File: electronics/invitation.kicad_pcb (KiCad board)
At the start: 2 copper layers, 86 x 57 mm, 53 parts, among them P1 USB Micro B, P10 Up Arrow, P11 Down Arrow, P2 Home btn, P3 Bottom Connections 1, P4 Left Arrow, P5 Right Arrow, P8 CONN_01X01, P9 CONN_01X02, U1 ATMEGA32U4-A, Y1 16 FA-238 Mhz

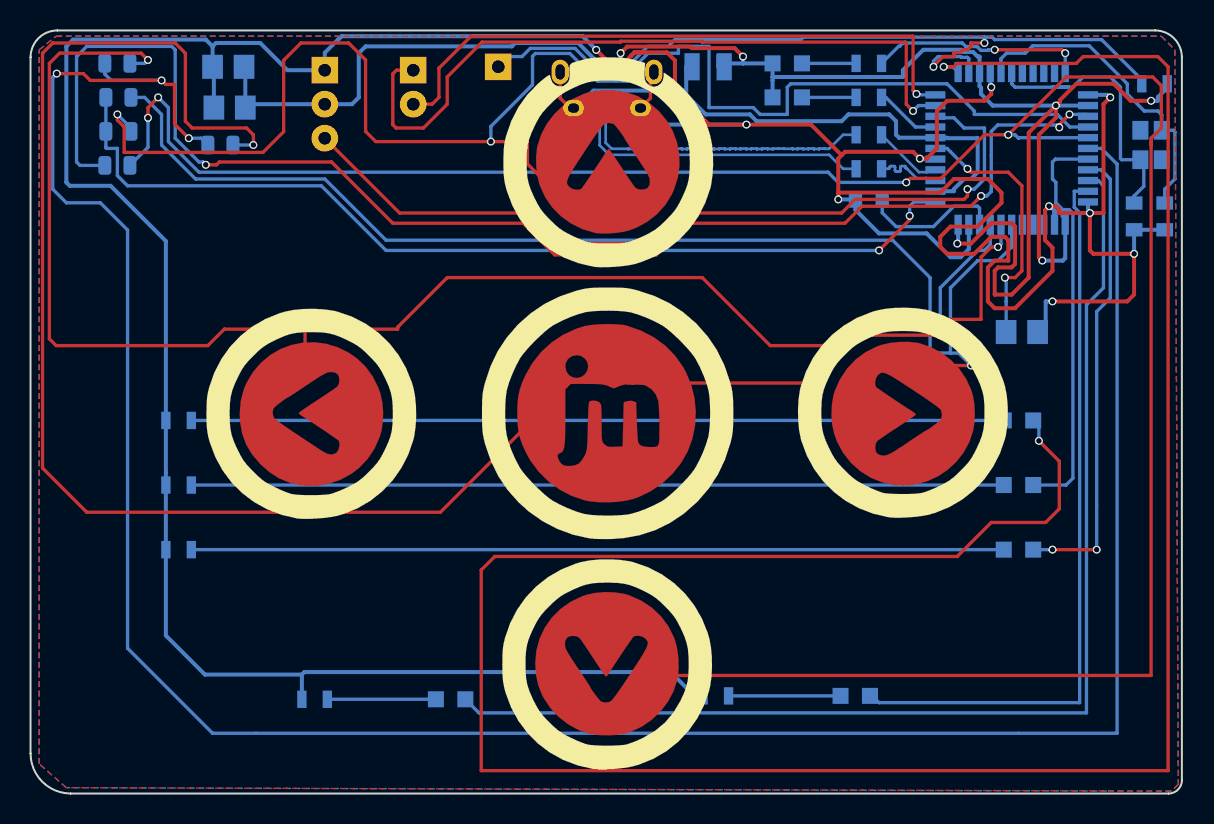
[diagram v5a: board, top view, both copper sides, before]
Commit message: Updated npm modules + code splitting functionality, found that the youtube chrome iOS bug is for all websites (hopefully this will be fixed by them soon), electronic card v13 submitted - To complete 1. Test that appropriate content appears on all devices - fix gyroscope movement on mobile devices 2. Create content for instruction page on headset webvr + mobile webvr + mobile + laptop 3. Test electronic card
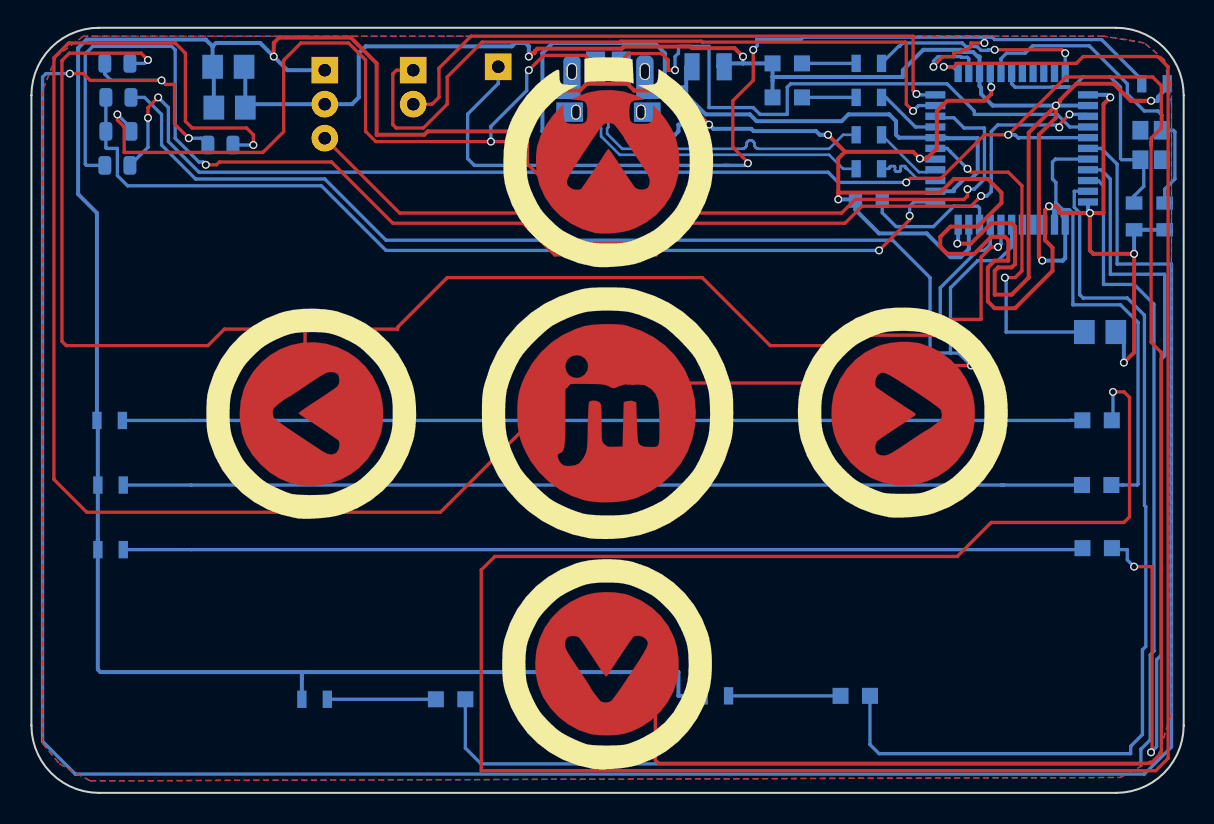
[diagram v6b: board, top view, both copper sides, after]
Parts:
- removed the G*** at (175.5, 120.9)
- removed the G*** at (162.3, 99.8)
- removed the G*** at (145.5, 121.2)
- added G***: LOGO, newAssets:jmSmallLogo, B.Cu at (155.4, 110.0)
- added G***: LOGO, newAssets:smallArrow, B.Cu at (148.5, 105.1)
- added G***: LOGO, newAssets:smallArrow, B.Cu at (146.0, 105.1)
- added G***: LOGO, newAssets:smallArrow, B.Cu at (143.4, 105.0)
- added G***: LOGO, newAssets:smallArrow, B.Cu at (140.8, 105.0)
- added G***: LOGO, newAssets:mail, B.Cu at (175.5, 120.9)
- added G***: LOGO, newAssets:phoneNew, B.Cu at (145.3, 121.2)
- added G***: LOGO, newAssets:front-background-three, F.Cu at (162.3, 99.8)
- P1: footprint Connect:USB_Micro-B -> 10103594-0001LF:FCI_10103594-0001LF
- moved D3 5.88 mm to (198.9, 109.9)
- moved D1 5.87 mm to (198.9, 100.3)
- moved D2 5.84 mm to (198.9, 105.2)
- moved C0 5.84 mm to (199.1, 93.7)
- moved R1 5.15 mm to (125.2, 100.3)
- moved R2 5.08 mm to (125.2, 105.2)
- moved R3 5.08 mm to (125.2, 110.0)
- moved P1 1.17 mm to (162.4, 74.3)
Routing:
- net interactLED: track 34.8 -> 67.2 mm
- net homeBtn: track 189.2 -> 207.8 mm
- net RESET: track 61.7 -> 80.0 mm, vias 2 -> 4
- net USBVCC: track 41.6 -> 58.7 mm
- net emailLED: track 55.3 -> 71.0 mm
- net downArrSens: track 182.7 -> 197.1 mm
- net phoneLED: track 88.0 -> 102.4 mm
- net Net-(P1-Pad6): track 11.5 -> 0.00 mm
- net Net-(D1-Pad1): track 60.7 -> 72.1 mm
- net Net-(D2-Pad1): track 60.7 -> 71.8 mm
- net Net-(D3-Pad1): track 60.7 -> 71.7 mm
- net powerLED: track 190.0 -> 199.5 mm
- net GND: track 295.4 -> 302.8 mm, vias 10 -> 11
- net Net-(C0-Pad1): track 19.6 -> 25.4 mm
- net upArrSens: track 116.6 -> 120.4 mm, vias 2 -> 4
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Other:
- board size 86 x 57 mm -> 86.1 x 57.2 mm
- board text added: "Plug this card into a USB port on your computer with the provided magnetic cable Open in a browser & explore by tapping frontside icons Activate content on screen by tapping the central icon on this card’s frontside"
- board text removed: "Connect this card to your PC with a USB cable Open in a web browser Tap the icons on this card’s reverse side"
- board text removed: "www.jamesmiller.design"

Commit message: Tested, updated and ordered multiples of the PCB, created CTA for split screen videos
- To do
a) assemble multiples
c) update website’s small bugs & UX issues
	1) fix on (digital design’s) large screen
	2) make all clicks add to router history (depending on how difficult this is!)
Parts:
- removed the G*** at (155.4, 110.0)
- removed the G*** at (175.5, 120.9)
- removed the G*** at (145.3, 121.2)
- added G***: LOGO, newAssets:smallJMLogo, B.Cu at (155.4, 110.0)
- added G***: LOGO, newAssets:mailIcon, B.Cu at (175.5, 120.9)
- added G***: LOGO, newAssets:phoneIcon, B.Cu at (145.3, 121.2)
